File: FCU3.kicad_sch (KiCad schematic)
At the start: 0 parts

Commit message: First schematic draft complete
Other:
- removed sheet Power - Sequencing
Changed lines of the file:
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@@
-	)
-	(sheet
-		(at 340.36 313.69)
-		(size 35.56 5.08)
-		(exclude_from_sim no)
-		(in_bom yes)
-		(on_board yes)
-		(dnp no)
-		(stroke
-			(width 0.1524)
-			(type solid)
-		)
-		(fill
-			(color 0 0 0 0.0000)
-		)
-		(property "Sheetname" "Power - Sequencing"
-			(at 340.36 312.6609 0)
-			(effects
-				(font
-					(face "Times New Roman")
-					(size 1.905 1.905)
-					(bold yes)
-					(color 0 0 0 1)
-				)
-				(justify left bottom)
-			)
-		)
-		(property "Sheetfile" "Power - Sequencing.kicad_sch"
-			(at 341.63 314.96 0)
-			(effects
-				(font
-					(face "Arial")
-					(size 1.27 1.27)
-				)
-				(justify left top)
-			)
-		)
-		(instances
-			(project "FCU3"
-				(path "/f9e05184-c88b-4a88-ae9c-ab2bdb32be7c"
-					(page "8")
-				)
-			)
-		)
 	)
 	(sheet

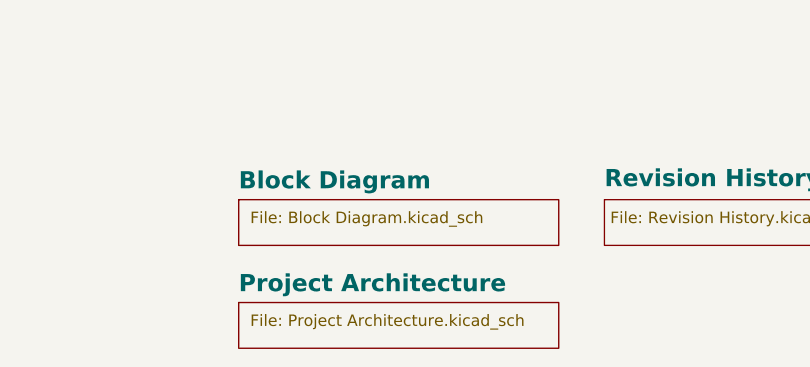
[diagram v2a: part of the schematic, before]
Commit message: Wiring Complete, ERC and DRC remaining
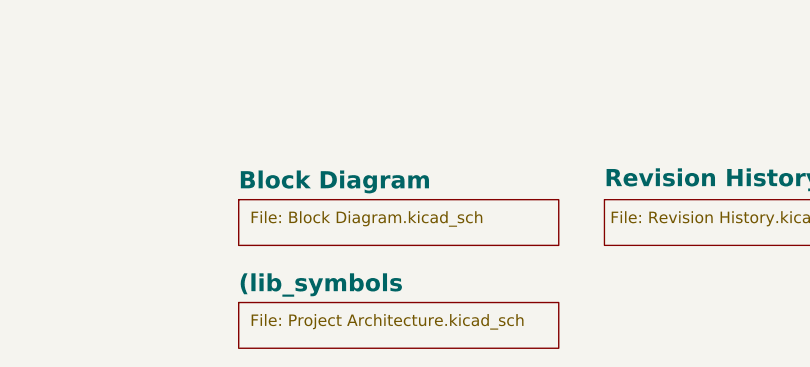
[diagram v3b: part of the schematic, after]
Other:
- sheet Project Architecture renamed (lib_symbols
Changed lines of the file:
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@@
 			(color 0 0 0 0.0000)
 		)
-		(property "Sheetname" "Project Architecture"
-			(at 299.72 312.6609 0)
-			(effects
-				(font
-					(face "Times New Roman")
-					(size 1.905 1.905)
-					(bold yes)
-					(color 0 0 0 1)
-				)
-				(justify left bottom)
-			)
-		)
-		(property "Sheetfile" "Project Architecture.kicad_sch"
-			(at 300.99 314.96 0)
-			(effects
-				(font
-					(face "Arial")
-					(size 1.27 1.27)
-				)
-				(justify left top)
-			)
-		)
-		(instances
-			(project "FCU3"
-				(path "/f9e05184-c88b-4a88-ae9c-ab2bdb32be7c"
-					(page "3")
-				)
-			)
-		)
-	)
 	(sheet_instances
 		(path "/"

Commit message: Modularized BEC and fixed generic components in schematic.
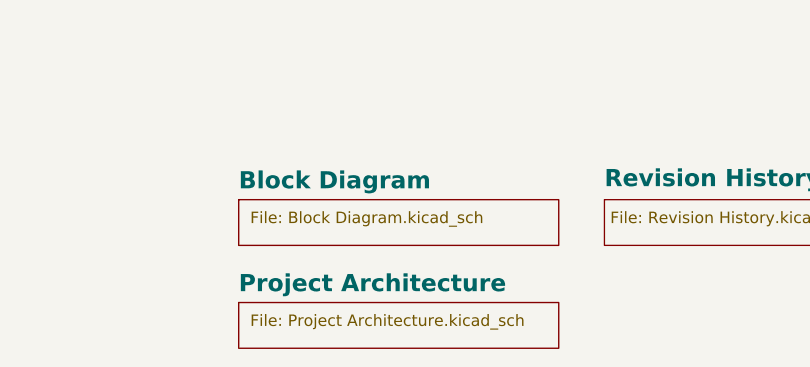
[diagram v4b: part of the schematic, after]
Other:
- sheet (lib_symbols renamed Project Architecture
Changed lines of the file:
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@@
 			(color 0 0 0 0.0000)
 		)
+		(property "Sheetname" "Project Architecture"
+			(at 299.72 312.6609 0)
+			(effects
+				(font
+					(face "Times New Roman")
+					(size 1.905 1.905)
+					(bold yes)
+					(color 0 0 0 1)
+				)
+				(justify left bottom)
+			)
+		)
+		(property "Sheetfile" "Project Architecture.kicad_sch"
+			(at 300.99 314.96 0)
+			(effects
+				(font
+					(face "Arial")
+					(size 1.27 1.27)
+				)
+				(justify left top)
+			)
+		)
+		(instances
+			(project "FCU3"
+				(path "/f9e05184-c88b-4a88-ae9c-ab2bdb32be7c"
+					(page "3")
+				)
+			)
+		)
+	)
 	(sheet_instances
 		(path "/"
